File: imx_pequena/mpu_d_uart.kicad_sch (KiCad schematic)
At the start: 4 parts, among them U1 MCIMX6Z0DVM09AB

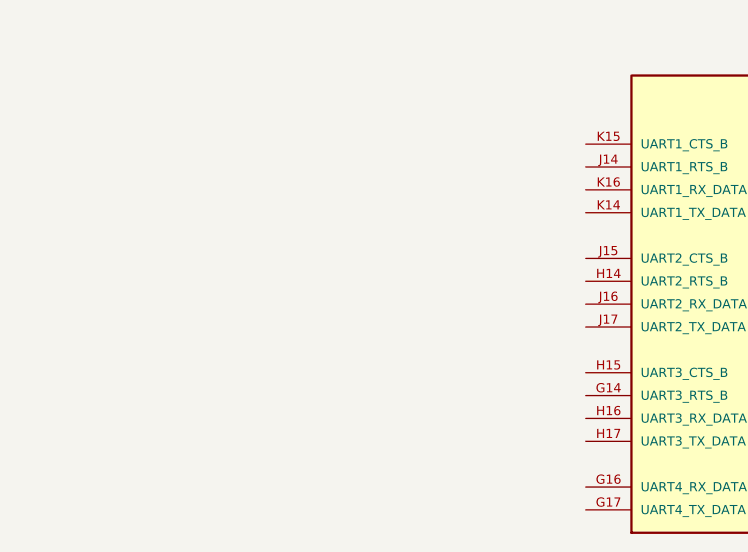
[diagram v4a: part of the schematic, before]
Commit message: Updated pinouts
Added misc uart changes
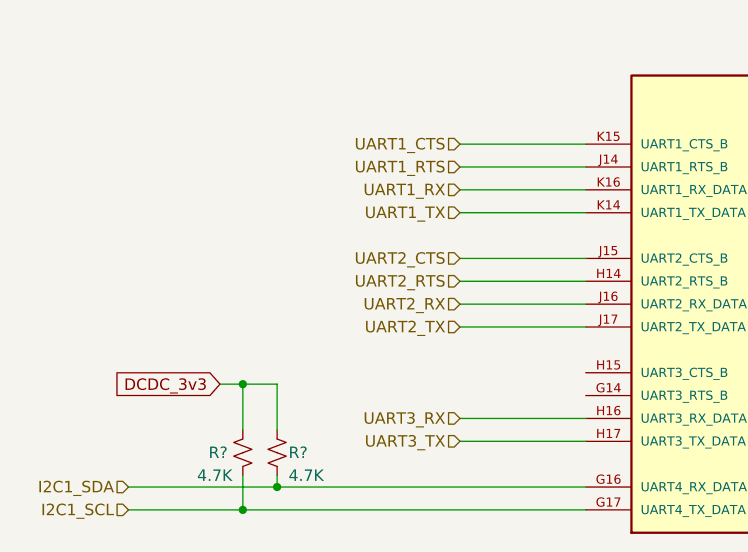
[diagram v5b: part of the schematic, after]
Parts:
- added R? (x2): 4.7K, symbol Device:R_Small_US
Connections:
- net I2C1_SDA: now reaches U1.G16 (UART4_RX_DATA)
- net I2C1_SDA: now also R?.2
- net I2C1_SCL: now reaches U1.G17 (UART4_TX_DATA)
- net I2C1_SCL: now also R?.2
- net UART2_RTS: now reaches U1.H14 (UART2_RTS_B)
- net UART3_RX: now reaches U1.H16 (UART3_RX_DATA)
- net UART3_TX: now reaches U1.H17 (UART3_TX_DATA)
- net UART1_RTS: now reaches U1.J14 (UART1_RTS_B)
- net UART2_CTS: now reaches U1.J15 (UART2_CTS_B)
- net UART2_RX: now reaches U1.J16 (UART2_RX_DATA)
- net UART2_TX: now reaches U1.J17 (UART2_TX_DATA)
- net UART1_TX: now reaches U1.K14 (UART1_TX_DATA)
- net UART1_CTS: now reaches U1.K15 (UART1_CTS_B)
- net UART1_RX: now reaches U1.K16 (UART1_RX_DATA)
- new net DCDC_3v3: R?.1, R?.1
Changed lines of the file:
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@@
   (junction (at 175.26 62.23) (diameter 0) (color 0 0 0 0)
   )
+  (junction (at 64.77 85.09) (diameter 0) (color 0 0 0 0)
+  )
   (junction (at 179.07 53.34) (diameter 0) (color 0 0 0 0)
   )
+  (junction (at 64.77 99.06) (diameter 0) (color 0 0 0 0)
+  )
   (junction (at 170.18 53.34) (diameter 0) (color 0 0 0 0)
   )
+  (junction (at 68.58 96.52) (diameter 0) (color 0 0 0 0)
+  )
   (wire (pts (xy 175.26 62.23) (xy 179.07 62.23))
     (stroke (width 0) (type default) (color 0 0 0 0))
   )
+  (wire (pts (xy 88.9 73.66) (xy 102.87 73.66))
+    (stroke (width 0) (type default) (color 0 0 0 0))
+  )
+  (wire (pts (xy 64.77 99.06) (xy 102.87 99.06))
+    (stroke (width 0) (type default) (color 0 0 0 0))
+  )
   (wire (pts (xy 170.18 53.34) (xy 179.07 53.34))
     (stroke (width 0) (type default) (color 0 0 0 0))
   )
+  (wire (pts (xy 52.07 96.52) (xy 68.58 96.52))
+    (stroke (width 0) (type default) (color 0 0 0 0))
+  )
+  (wire (pts (xy 88.9 78.74) (xy 102.87 78.74))
+    (stroke (width 0) (type default) (color 0 0 0 0))
+  )
+  (wire (pts (xy 68.58 90.17) (xy 68.58 85.09))
+    (stroke (width 0) (type default) (color 0 0 0 0))
+  )
+  (wire (pts (xy 88.9 58.42) (xy 102.87 58.42))
+    (stroke (width 0) (type default) (color 0 0 0 0))
+  )
+  (wire (pts (xy 68.58 85.09) (xy 64.77 85.09))
+    (stroke (width 0) (type default) (color 0 0 0 0))
+  )
   (wire (pts (xy 179.07 53.34) (xy 180.34 53.34))
     (stroke (width 0) (type default) (color 0 0 0 0))
@@
     (stroke (width 0) (type default) (color 0 0 0 0))
   )
+  (wire (pts (xy 52.07 99.06) (xy 64.77 99.06))
+    (stroke (width 0) (type default) (color 0 0 0 0))
+  )
   (wire (pts (xy 185.42 53.34) (xy 189.23 53.34))
     (stroke (width 0) (type default) (color 0 0 0 0))
   )
+  (wire (pts (xy 68.58 96.52) (xy 102.87 96.52))
+    (stroke (width 0) (type default) (color 0 0 0 0))
+  )
+  (wire (pts (xy 88.9 66.04) (xy 102.87 66.04))
+    (stroke (width 0) (type default) (color 0 0 0 0))
+  )
   (wire (pts (xy 170.18 53.34) (xy 170.18 54.61))
     (stroke (width 0) (type default) (color 0 0 0 0))
   )
+  (wire (pts (xy 88.9 91.44) (xy 102.87 91.44))
+    (stroke (width 0) (type default) (color 0 0 0 0))
+  )
+  (wire (pts (xy 88.9 88.9) (xy 102.87 88.9))
+    (stroke (width 0) (type default) (color 0 0 0 0))
+  )
+  (wire (pts (xy 88.9 71.12) (xy 102.87 71.12))
+    (stroke (width 0) (type default) (color 0 0 0 0))
+  )
+  (wire (pts (xy 88.9 60.96) (xy 102.87 60.96))
+    (stroke (width 0) (type default) (color 0 0 0 0))
+  )
+  (wire (pts (xy 88.9 76.2) (xy 102.87 76.2))
+    (stroke (width 0) (type default) (color 0 0 0 0))
+  )
+  (wire (pts (xy 64.77 90.17) (xy 64.77 85.09))
+    (stroke (width 0) (type default) (color 0 0 0 0))
+  )
   (wire (pts (xy 163.83 53.34) (xy 170.18 53.34))
     (stroke (width 0) (type default) (color 0 0 0 0))
   )
+  (wire (pts (xy 68.58 96.52) (xy 68.58 95.25))
+    (stroke (width 0) (type default) (color 0 0 0 0))
+  )
   (wire (pts (xy 179.07 59.69) (xy 179.07 62.23))
     (stroke (width 0) (type default) (color 0 0 0 0))
   )
+  (wire (pts (xy 88.9 63.5) (xy 102.87 63.5))
+    (stroke (width 0) (type default) (color 0 0 0 0))
+  )
   (wire (pts (xy 179.07 53.34) (xy 179.07 54.61))
     (stroke (width 0) (type default) (color 0 0 0 0))
   )
+  (wire (pts (xy 64.77 99.06) (xy 64.77 95.25))
+    (stroke (width 0) (type default) (color 0 0 0 0))
+  )
   (wire (pts (xy 170.18 62.23) (xy 175.26 62.23))
+    (stroke (width 0) (type default) (color 0 0 0 0))
+  )
+  (wire (pts (xy 64.77 85.09) (xy 62.23 85.09))
     (stroke (width 0) (type default) (color 0 0 0 0))
   )
@@
     )
   )
+  (global_label "DCDC_3v3" (shape input) (at 62.23 85.09 180) (fields_autoplaced)
+    (effects (font (size 1.27 1.27)) (justify right))
+    (property "Intersheet References" "${INTERSHEET_REFS}" (id 0) (at 50.3826 85.0106 0)
+      (effects (font (size 1.27 1.27)) (justify right) hide)
+    )
+  )
+  (hierarchical_label "UART1_RTS" (shape input) (at 88.9 60.96 180)
+    (effects (font (size 1.27 1.27)) (justify right))
+  )
+  (hierarchical_label "I2C1_SDA" (shape input) (at 52.07 96.52 180)
+    (effects (font (size 1.27 1.27)) (justify right))
+  )
+  (hierarchical_label "UART1_RX" (shape input) (at 88.9 63.5 180)
+    (effects (font (size 1.27 1.27)) (justify right))
+  )
+  (hierarchical_label "UART2_RX" (shape input) (at 88.9 76.2 180)
+    (effects (font (size 1.27 1.27)) (justify right))
+  )
+  (hierarchical_label "UART3_RX" (shape input) (at 88.9 88.9 180)
+    (effects (font (size 1.27 1.27)) (justify right))
+  )
+  (hierarchical_label "UART3_TX" (shape input) (at 88.9 91.44 180)
+    (effects (font (size 1.27 1.27)) (justify right))
+  )
+  (hierarchical_label "UART1_TX" (shape input) (at 88.9 66.04 180)
+    (effects (font (size 1.27 1.27)) (justify right))
+  )
+  (hierarchical_label "UART2_CTS" (shape input) (at 88.9 71.12 180)
+    (effects (font (size 1.27 1.27)) (justify right))
+  )
+  (hierarchical_label "I2C1_SCL" (shape input) (at 52.07 99.06 180)
+    (effects (font (size 1.27 1.27)) (justify right))
+  )
+  (hierarchical_label "UART2_TX" (shape input) (at 88.9 78.74 180)
+    (effects (font (size 1.27 1.27)) (justify right))
+  )
+  (hierarchical_label "UART2_RTS" (shape input) (at 88.9 73.66 180)
+    (effects (font (size 1.27 1.27)) (justify right))
+  )
+  (hierarchical_label "UART1_CTS" (shape input) (at 88.9 58.42 180)
+    (effects (font (size 1.27 1.27)) (justify right))
+  )
   (symbol (lib_id "power:GND") (at 175.26 62.23 0) (unit 1)
     (in_bom yes) (on_board yes) (fields_autoplaced)
@@
     (pin "1")
   )
+  (symbol (lib_id "Device:R_Small_US") (at 68.58 92.71 0) (unit 1)
+    (in_bom yes) (on_board yes)
+    (property "Reference" "R?" (id 0) (at 69.85 92.71 0)
+      (effects (font (size 1.27 1.27)) (justify left))
+    )
+    (property "Value" "4.7K" (id 1) (at 69.85 95.25 0)
+      (effects (font (size 1.27 1.27)) (justify left))
+    )
+    (property "Footprint" "" (id 2) (at 68.58 92.71 0)
+      (effects (font (size 1.27 1.27)) hide)
+    )
+    (property "Datasheet" "~" (id 3) (at 68.58 92.71 0)
+      (effects (font (size 1.27 1.27)) hide)
+    )
+    (pin "1")
+    (pin "2")
+  )
   (symbol (lib_id "Device:R_Small_US") (at 182.88 53.34 90) (unit 1)
     (in_bom yes) (on_board yes)
@@
       (effects (font (size 1.27 1.27)) hide)
     )
+    (pin "1")
+    (pin "2")
+  )
+  (symbol (lib_id "Device:R_Small_US") (at 64.77 92.71 0) (mirror y) (unit 1)
+    (in_bom yes) (on_board yes)
+    (property "Reference" "R?" (id 0) (at 60.96 92.71 0)
+      (effects (font (size 1.27 1.27)) (justify right))
+    )
+    (property "Value" "4.7K" (id 1) (at 59.69 95.25 0)
+      (effects (font (size 1.27 1.27)) (justify right))
+    )
+    (property "Footprint" "" (id 2) (at 64.77 92.71 0)
+      (effects (font (size 1.27 1.27)) hide)
+    )
+    (property "Datasheet" "~" (id 3) (at 64.77 92.71 0)
+      (effects (font (size 1.27 1.27)) hide)
+    )

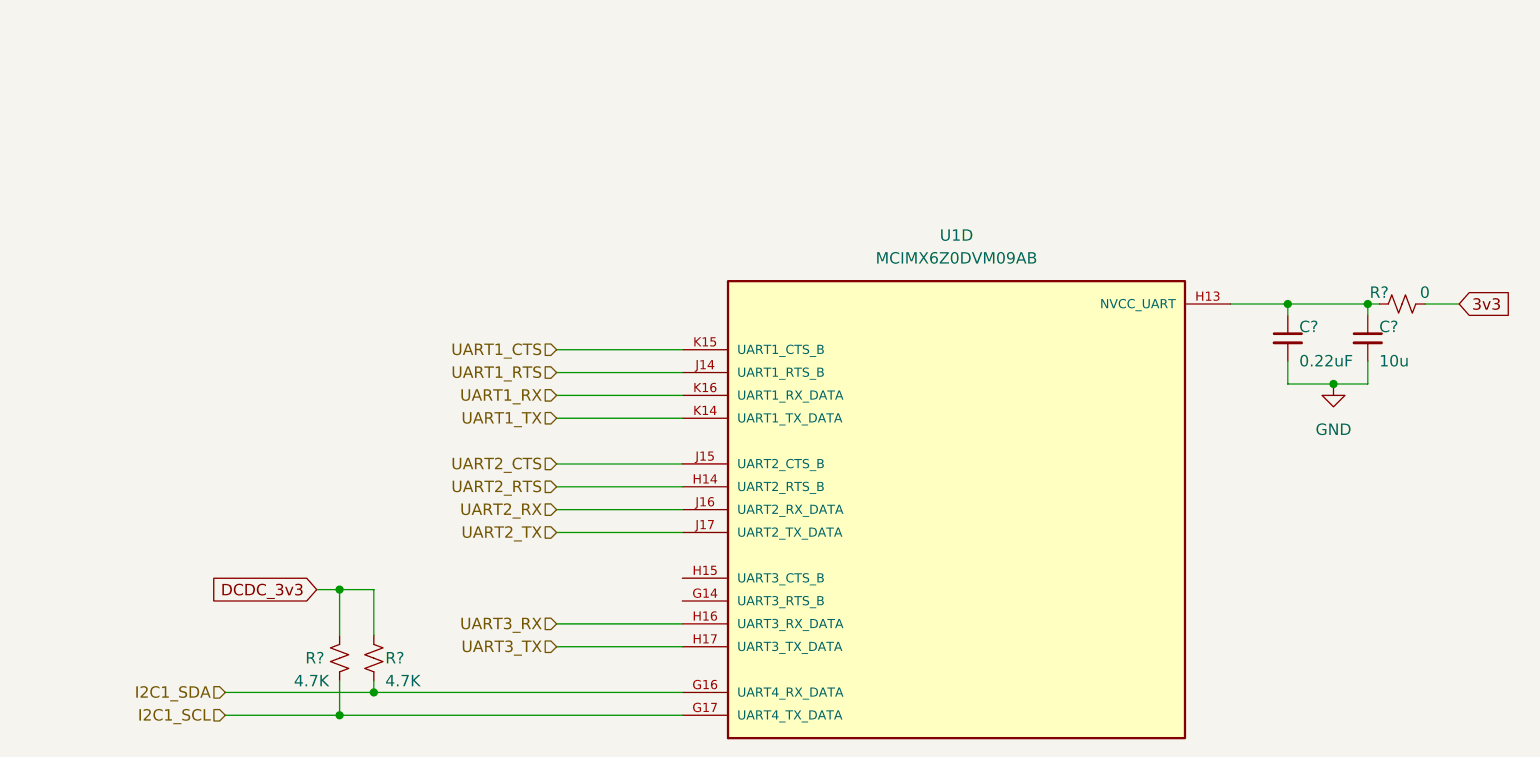
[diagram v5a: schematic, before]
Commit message: Part Assignment
Assigned GPIOs and assigned footprints to most parts
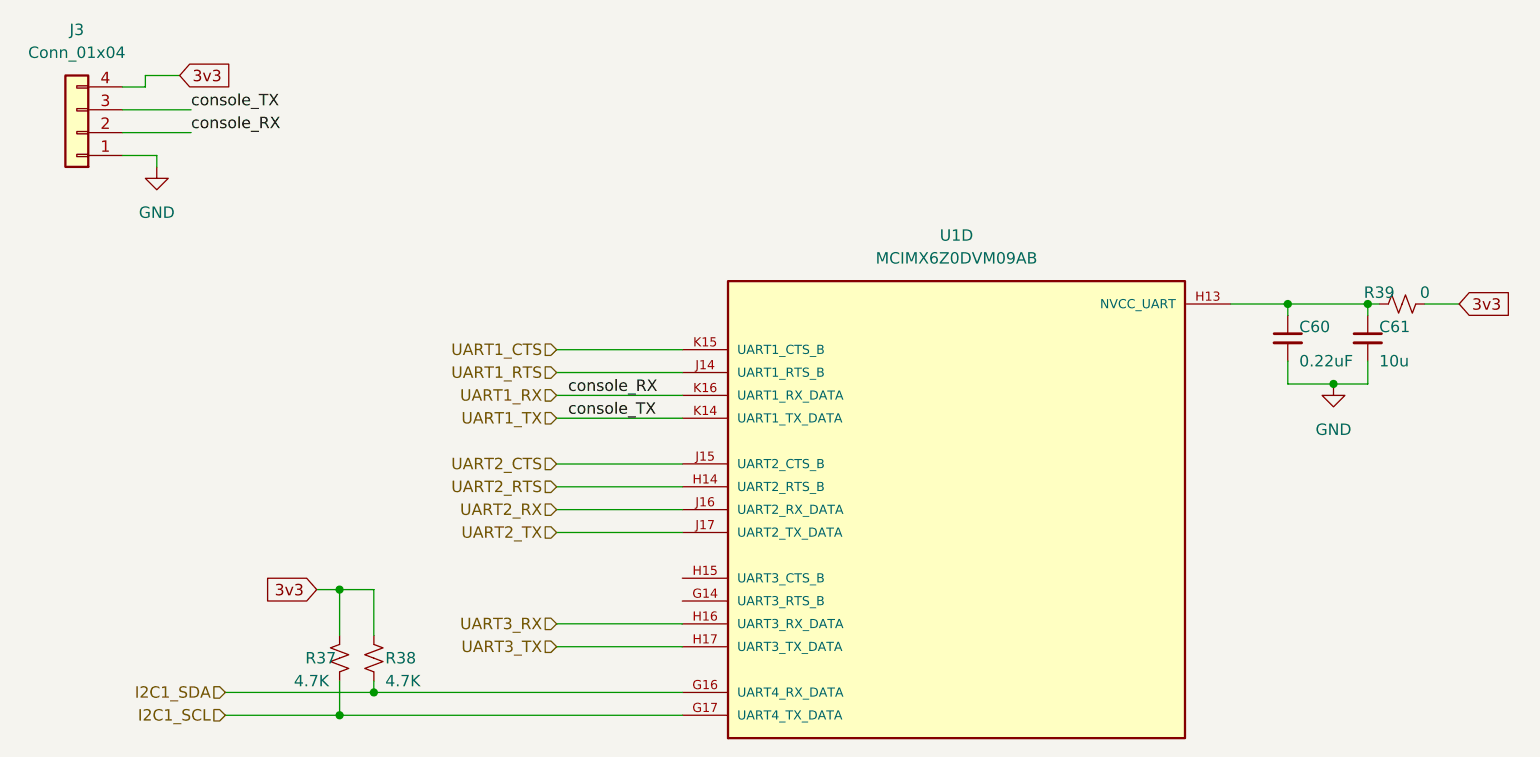
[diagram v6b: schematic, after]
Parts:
- added J3: Conn_01x04, Connector_PinHeader_2.54mm:PinHeader_1x04_P2.54mm_Vertical, symbol Connector_Generic:Conn_01x04
- C60: renamed from C?; footprint (none) -> Capacitor_SMD:C_0402_1005Metric
- C61: renamed from C?; footprint (none) -> Capacitor_SMD:C_0805_2012Metric
- R37, R38, R39: renamed from R?; footprint (none) -> Resistor_SMD:R_0402_1005Metric
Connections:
- net DCDC_3v3 is gone; now on net 3v3: R37.1, R38.1
- net 3v3: now also J3.4 (Pin_4)
- net GND: now also J3.1 (Pin_1)
- net UART1_RX: now also J3.2 (Pin_2)
- net UART1_TX: now also J3.3 (Pin_3)
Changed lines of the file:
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@@
+    (stroke (width 0) (type default) (color 0 0 0 0))
+  )
+  (wire (pts (xy 40.64 36.83) (xy 44.45 36.83))
     (stroke (width 0) (type default) (color 0 0 0 0))
   )
@@
     (stroke (width 0) (type default) (color 0 0 0 0))
   )
+  (wire (pts (xy 40.64 31.75) (xy 48.26 31.75))
+    (stroke (width 0) (type default) (color 0 0 0 0))
+  )
   (wire (pts (xy 68.58 85.09) (xy 64.77 85.09))
     (stroke (width 0) (type default) (color 0 0 0 0))
@@
     (stroke (width 0) (type default) (color 0 0 0 0))
   )
+  (wire (pts (xy 43.18 27.94) (xy 43.18 29.21))
+    (stroke (width 0) (type default) (color 0 0 0 0))
+  )
   (wire (pts (xy 170.18 59.69) (xy 170.18 62.23))
     (stroke (width 0) (type default) (color 0 0 0 0))
@@
     (stroke (width 0) (type default) (color 0 0 0 0))
   )
+  (wire (pts (xy 44.45 36.83) (xy 44.45 38.1))
+    (stroke (width 0) (type default) (color 0 0 0 0))
+  )
+  (wire (pts (xy 40.64 29.21) (xy 43.18 29.21))
+    (stroke (width 0) (type default) (color 0 0 0 0))
+  )
   (wire (pts (xy 88.9 66.04) (xy 102.87 66.04))
     (stroke (width 0) (type default) (color 0 0 0 0))
@@
     (stroke (width 0) (type default) (color 0 0 0 0))
   )
+  (wire (pts (xy 40.64 34.29) (xy 48.26 34.29))
+    (stroke (width 0) (type default) (color 0 0 0 0))
+  )
   (wire (pts (xy 64.77 90.17) (xy 64.77 85.09))
     (stroke (width 0) (type default) (color 0 0 0 0))
@@
     (stroke (width 0) (type default) (color 0 0 0 0))
   )
+  (wire (pts (xy 46.99 27.94) (xy 43.18 27.94))
+    (stroke (width 0) (type default) (color 0 0 0 0))
+  )
   (wire (pts (xy 179.07 59.69) (xy 179.07 62.23))
     (stroke (width 0) (type default) (color 0 0 0 0))
@@
   (wire (pts (xy 64.77 85.09) (xy 62.23 85.09))
     (stroke (width 0) (type default) (color 0 0 0 0))
+  )
+  (label "console_TX" (at 90.17 66.04 0)
+    (effects (font (size 1.27 1.27)) (justify left bottom))
+  )
+  (label "console_RX" (at 90.17 63.5 0)
+    (effects (font (size 1.27 1.27)) (justify left bottom))
+  )
+  (label "console_TX" (at 48.26 31.75 0)
+    (effects (font (size 1.27 1.27)) (justify left bottom))
+  )
+  (label "console_RX" (at 48.26 34.29 0)
+    (effects (font (size 1.27 1.27)) (justify left bottom))
   )
   (global_label "3v3" (shape input) (at 189.23 53.34 0) (fields_autoplaced)
@@
     )
   )
-  (global_label "DCDC_3v3" (shape input) (at 62.23 85.09 180) (fields_autoplaced)
-    (effects (font (size 1.27 1.27)) (justify right))
-    (property "Intersheet References" "${INTERSHEET_REFS}" (id 0) (at 50.3826 85.0106 0)
+  (global_label "3v3" (shape input) (at 46.99 27.94 0) (fields_autoplaced)
+    (effects (font (size 1.27 1.27)) (justify left))
+    (property "Intersheet References" "${INTERSHEET_REFS}" (id 0) (at 52.7898 27.8606 0)
+      (effects (font (size 1.27 1.27)) (justify left) hide)
+    )
+  )
+  (global_label "3v3" (shape input) (at 62.23 85.09 180) (fields_autoplaced)
+    (effects (font (size 1.27 1.27)) (justify right))
+    (property "Intersheet References" "${INTERSHEET_REFS}" (id 0) (at 56.4302 85.1694 0)
       (effects (font (size 1.27 1.27)) (justify right) hide)
     )
@@
   (symbol (lib_id "power:GND") (at 175.26 62.23 0) (unit 1)
     (in_bom yes) (on_board yes) (fields_autoplaced)
-    (property "Reference" "#PWR?" (id 0) (at 175.26 68.58 0)
+    (property "Reference" "#PWR0152" (id 0) (at 175.26 68.58 0)
       (effects (font (size 1.27 1.27)) hide)
     )
@@
     (pin "1")
   )
+  (symbol (lib_id "power:GND") (at 44.45 38.1 0) (unit 1)
+    (in_bom yes) (on_board yes) (fields_autoplaced)
+    (property "Reference" "#PWR0151" (id 0) (at 44.45 44.45 0)
+      (effects (font (size 1.27 1.27)) hide)
+    )
+    (property "Value" "GND" (id 1) (at 44.45 43.18 0))
+    (property "Footprint" "" (id 2) (at 44.45 38.1 0)
+      (effects (font (size 1.27 1.27)) hide)
+    )
+    (property "Datasheet" "" (id 3) (at 44.45 38.1 0)
+      (effects (font (size 1.27 1.27)) hide)
+    )
+    (pin "1")
+  )
   (symbol (lib_id "Device:R_Small_US") (at 68.58 92.71 0) (unit 1)
     (in_bom yes) (on_board yes)
-    (property "Reference" "R?" (id 0) (at 69.85 92.71 0)
+    (property "Reference" "R38" (id 0) (at 69.85 92.71 0)
       (effects (font (size 1.27 1.27)) (justify left))
     )
@@
       (effects (font (size 1.27 1.27)) (justify left))
     )
-    (property "Footprint" "" (id 2) (at 68.58 92.71 0)
+    (property "Footprint" "Resistor_SMD:R_0402_1005Metric" (id 2) (at 68.58 92.71 0)
       (effects (font (size 1.27 1.27)) hide)
     )
@@
   (symbol (lib_id "Device:R_Small_US") (at 182.88 53.34 90) (unit 1)
     (in_bom yes) (on_board yes)
-    (property "Reference" "R?" (id 0) (at 180.34 52.07 90))
+    (property "Reference" "R39" (id 0) (at 180.34 52.07 90))
     (property "Value" "0" (id 1) (at 185.42 52.07 90))
-    (property "Footprint" "" (id 2) (at 182.88 53.34 0)
+    (property "Footprint" "Resistor_SMD:R_0402_1005Metric" (id 2) (at 182.88 53.34 0)
       (effects (font (size 1.27 1.27)) hide)
     )
@@
     (pin "2")
   )
+  (symbol (lib_id "Connector_Generic:Conn_01x04") (at 35.56 34.29 180) (unit 1)
+    (in_bom yes) (on_board yes) (fields_autoplaced)
+    (property "Reference" "J3" (id 0) (at 35.56 22.86 0))
+    (property "Value" "Conn_01x04" (id 1) (at 35.56 25.4 0))
+    (property "Footprint" "Connector_PinHeader_2.54mm:PinHeader_1x04_P2.54mm_Vertical" (id 2) (at 35.56 34.29 0)
+      (effects (font (size 1.27 1.27)) hide)
+    )
+    (property "Datasheet" "~" (id 3) (at 35.56 34.29 0)
+      (effects (font (size 1.27 1.27)) hide)
+    )
+    (pin "1")
+    (pin "2")
+    (pin "3")
+    (pin "4")
+  )
   (symbol (lib_id "Device:C_Small") (at 179.07 57.15 0) (unit 1)
     (in_bom yes) (on_board yes)
-    (property "Reference" "C?" (id 0) (at 180.34 55.88 0)
+    (property "Reference" "C61" (id 0) (at 180.34 55.88 0)
       (effects (font (size 1.27 1.27)) (justify left))
     )
@@
       (effects (font (size 1.27 1.27)) (justify left))
     )
-    (property "Footprint" "" (id 2) (at 179.07 57.15 0)
+    (property "Footprint" "Capacitor_SMD:C_0805_2012Metric" (id 2) (at 179.07 57.15 0)
       (effects (font (size 1.27 1.27)) hide)
     )
@@
   (symbol (lib_id "Device:R_Small_US") (at 64.77 92.71 0) (mirror y) (unit 1)
     (in_bom yes) (on_board yes)
-    (property "Reference" "R?" (id 0) (at 60.96 92.71 0)
+    (property "Reference" "R37" (id 0) (at 60.96 92.71 0)
       (effects (font (size 1.27 1.27)) (justify right))
     )
@@
       (effects (font (size 1.27 1.27)) (justify right))
     )
-    (property "Footprint" "" (id 2) (at 64.77 92.71 0)
+    (property "Footprint" "Resistor_SMD:R_0402_1005Metric" (id 2) (at 64.77 92.71 0)
       (effects (font (size 1.27 1.27)) hide)
     )
@@
   (symbol (lib_id "Device:C_Small") (at 170.18 57.15 0) (unit 1)
     (in_bom yes) (on_board yes)
-    (property "Reference" "C?" (id 0) (at 171.45 55.88 0)
+    (property "Reference" "C60" (id 0) (at 171.45 55.88 0)
       (effects (font (size 1.27 1.27)) (justify left))
     )
@@
       (effects (font (size 1.27 1.27)) (justify left))
     )
-    (property "Footprint" "" (id 2) (at 170.18 57.15 0)
-      (effects (font (size 1.27 1.27)) hide)
-    )
+    (property "Footprint" "Capacitor_SMD:C_0402_1005Metric" (id 2) (at 170.18 57.15 0)
+      (effects (font (size 1.27 1.27)) hide)
+    )
